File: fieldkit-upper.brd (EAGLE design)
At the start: 96 x 62 mm, 52 parts, among them J1 TAG-CONNECT, U1 TC58CVG1S3HRAIG, U2 TC58CVG1S3HRAIG, U3 TC58CVG1S3HRAIG, U4 TC58CVG1S3HRAIG

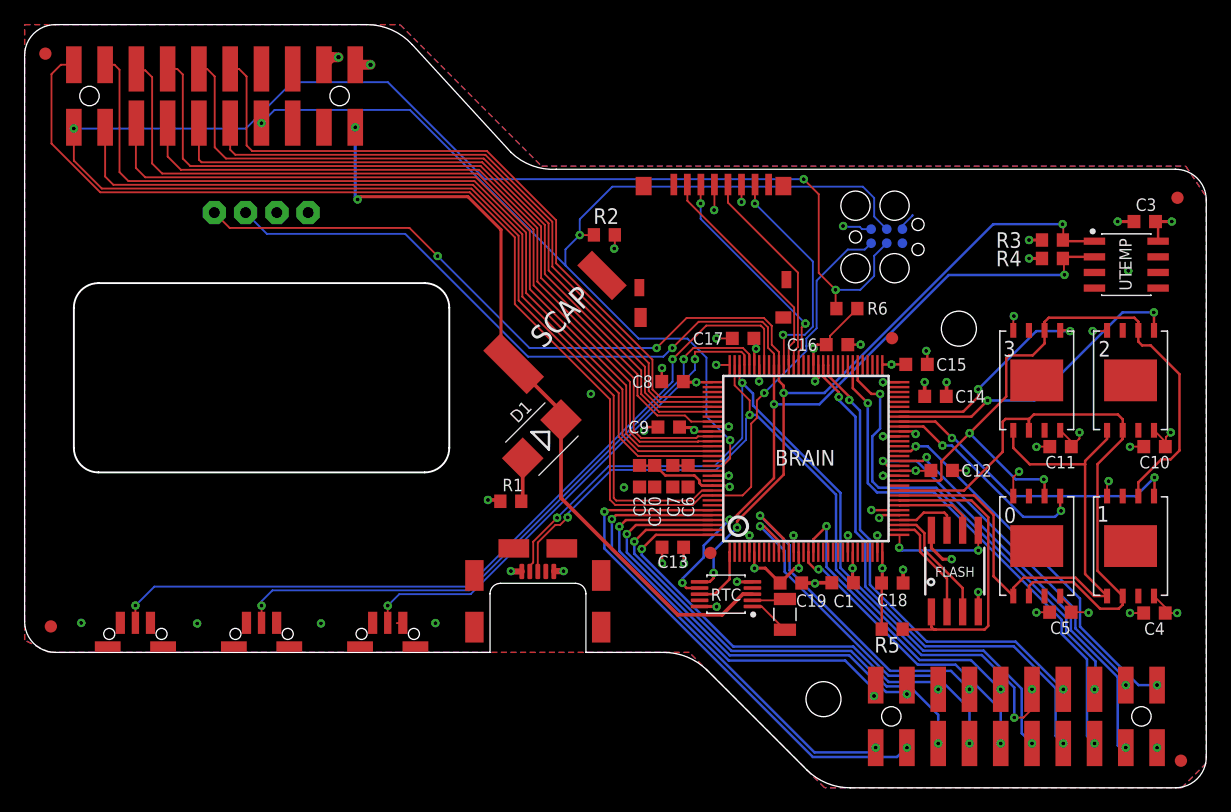
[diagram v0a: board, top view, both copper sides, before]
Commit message: Schematic readability overhaul, repo look & feel.
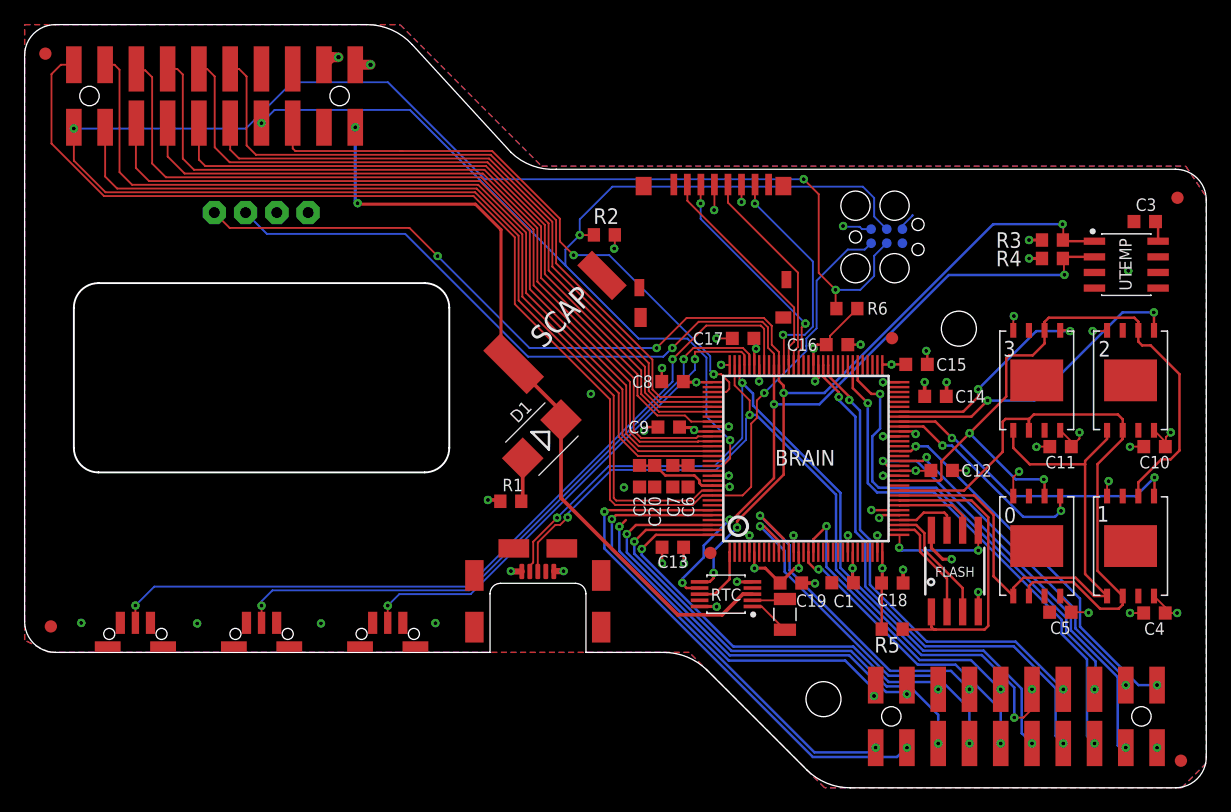
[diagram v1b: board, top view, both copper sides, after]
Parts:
- C1, C10, C11, C12, C13, C14, C15, C16, C17, C18, C19, C2, C20, C3, C4, C5, C8, C9: device rcl:C0603K -> Conservify:C0603K
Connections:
- net MOD_G10 renamed WIFI_RESET
- net MOD_G11 renamed WIFI_IRQ
- net MOD_G12 renamed BATTERY_CHARGING
- net MOD_G13 renamed RAD_G2
- net MOD_G14 renamed RAD_G3
- net MOD_G4 renamed WAKE_BUTTON
- net MOD_G6 renamed GPS_ENABLE
- net MOD_G7 renamed WIFI_ENABLE
- net MOD_G8 renamed WIFI_WAKE
- net MOD_G9 renamed WIFI_CS
- removed net UPPER_PIN13: UPPER.PIN13
- removed net UPPER_PIN14: UPPER.PIN14
- removed net UPPER_PIN8: UPPER.PIN8
- removed net UPPER_PIN9: UPPER.PIN9
- new net BP_ENABLE: BRAIN.99, UPPER.PIN8
- new net MOD_G1: BRAIN.127, LOWER.PIN13
- new net RAD_G1: BRAIN.125
- net 3V3: now also SCREEN.0, U1.8, U2.8, U3.8, U4.8; no longer SCREEN.P0, U1.P$8, U2.P$8, U3.P$8, U4.P$8
- net CORE_SCL: now also SCREEN.2; no longer SCREEN.P2
- net CORE_SDA: now also SCREEN.3; no longer SCREEN.P3
- net FLASH_MISO: now also U1.2, U2.2, U3.2, U4.2; no longer U1.P$2, U2.P$2, U3.P$2, U4.P$2
- net FLASH_MOSI: now also U1.5, U2.5, U3.5, U4.5; no longer U1.P$5, U2.P$5, U3.P$5, U4.P$5
- net FLASH_S0: now also U1.1; no longer U1.P$1
- net FLASH_S1: now also U2.1; no longer U2.P$1
- net FLASH_S2: now also U3.1; no longer U3.P$1
- net FLASH_S3: now also U4.1; no longer U4.P$1
- net FLASH_SCK: now also U1.6, U2.6, U3.6, U4.6; no longer U1.P$6, U2.P$6, U3.P$6, U4.P$6
- net GND: now also SCREEN.1, SD.PAD1, SD.PAD2, SD.PAD3, SD.PAD4, SD.PAD5, SD.PAD6, U1.4, U2.4, U3.4, U4.4, USB.PAD1, USB.PAD2, USB.PAD3, USB.PAD4, USB.PAD5, USB.PAD6; no longer SCREEN.P1, U1.P$4, U2.P$4, U3.P$4, U4.P$4
- net MOD_G0: no longer BRAIN.125
- net MOD_G2: now also BRAIN.12; no longer BRAIN.127, LOWER.PIN13
- net MOD_G5: no longer BRAIN.12
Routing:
- net BP_ENABLE: track 0.00 -> 49.2 mm, vias 0 -> 2
- net MOD_G2: track 40.2 -> 0.00 mm, vias 2 -> 0
- net MOD_G1: track 0.00 -> 40.2 mm, vias 0 -> 2
- net MOD_G0: track 36.6 -> 29.6 mm
- net GND: track 53.1 -> 48.5 mm, vias 44 -> 42
- net 3V3: track 80.2 -> 78.3 mm, vias 29 -> 28
- net MOD_G5: track 27.8 -> 26.8 mm

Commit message: Routing cleanup, pin nomenclature fixes.
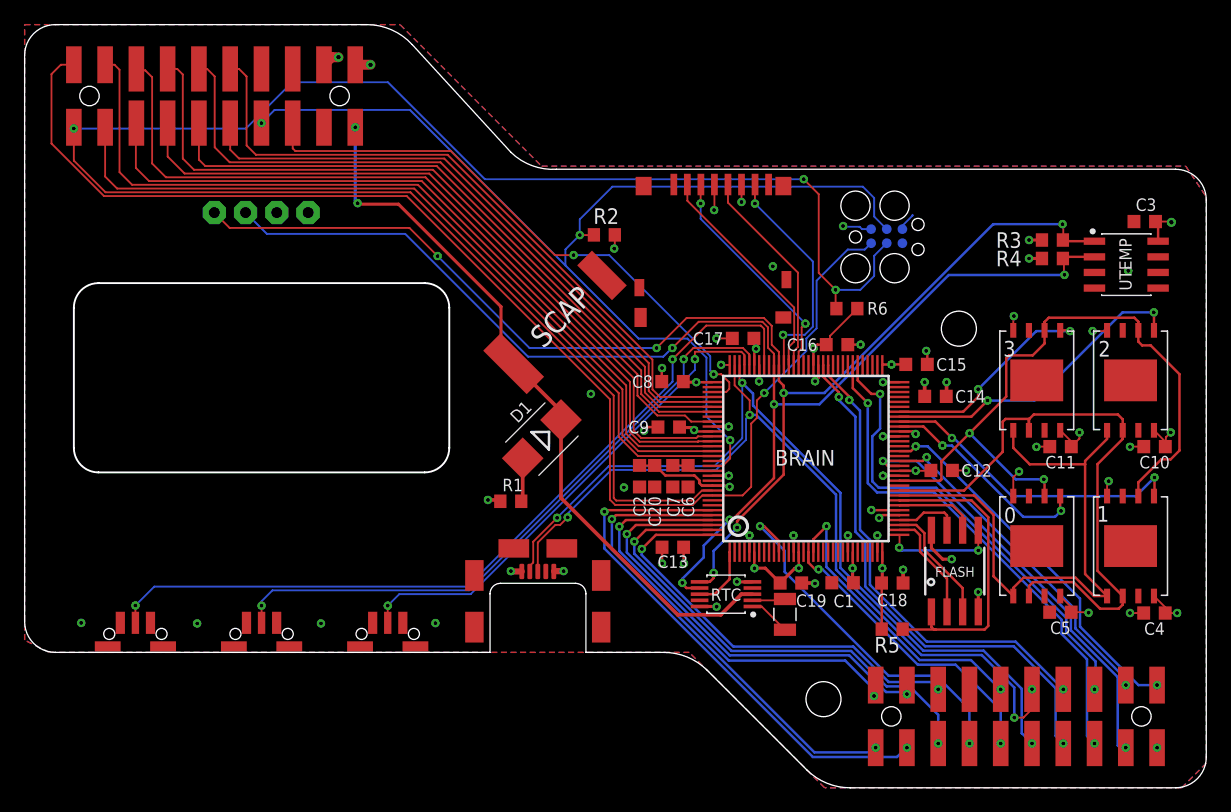
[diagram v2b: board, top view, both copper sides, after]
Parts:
- removed FID1, FID2, FID3, FID4, FID5, FID6: FIDUCIAL_1MM, microbuilder:FIDUCIAL_1MM
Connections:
- removed net MOD_G0: LOWER.PIN10
- net RAD_G1: now also LOWER.PIN10
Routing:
- net RAD_G1: track 0.00 -> 36.6 mm, vias 0 -> 2
- net MOD_G0: track 29.6 -> 0.00 mm, vias 2 -> 0
- net MOD_G5: track 26.8 -> 0.00 mm, vias 2 -> 0
- net VBACKUP: track 63.1 -> 59.4 mm
- net SWDIO: track 110.0 -> 106.8 mm
- net SWCLK: track 156.7 -> 153.7 mm
- net BATTERY_CHARGING: track 67.8 -> 64.8 mm
- net WIFI_IRQ: track 72.3 -> 69.4 mm
- net WIFI_RESET: track 64.9 -> 62.2 mm
- net WIFI_CS: track 68.5 -> 65.9 mm
- net WIFI_WAKE: track 61.6 -> 59.0 mm
- net RADIO_MISO: track 63.6 -> 61.1 mm
- net RADIO_SCK: track 56.6 -> 54.3 mm
- net RADIO_MOSI: track 59.9 -> 57.7 mm
- net GPS_RX: track 53.3 -> 51.2 mm
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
